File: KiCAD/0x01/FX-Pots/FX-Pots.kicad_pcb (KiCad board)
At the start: 2 copper layers, 100 x 100 mm, 41 parts, among them J1 IN, J2 OUT, SW1 SW_Push_LED, SW2 SW_Push_LED, SW3 SW_Push_LED, SW4 SW_Push_LED, SW5 SW_Push_LED, SW6 SW_Push_LED, SW7 SW_Push_LED, SW8 SW_Push_LED, U1 ADS7830, U2 HT16K33 24SOP

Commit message: fixes
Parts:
- U2: footprint Package_SO:SSOP-24_5.3x8.2mm_P0.65mm -> Package_SO:SOIC-24W_7.5x15.4mm_P1.27mm
- moved C2 2.68 mm to (153.0, 81.5)
- moved D2 1.69 mm to (152.5, 100.5)
- moved D3 1.69 mm to (154.6, 100.5)
- moved C3 0.49 mm to (154.2, 112.5)
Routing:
- net GND: track 132.0 -> 15.2 mm, vias 8 -> 4
- net +5V: track 70.3 -> 4.73 mm, vias 8 -> 3
- net /A1_H: track 85.9 -> 111.1 mm
- net /R3: track 107.9 -> 128.5 mm, vias 0 -> 1
- net /SDA: track 108.2 -> 125.5 mm
- net /POT7: track 59.5 -> 43.0 mm, vias 1 -> 0
- net /POT5: track 62.9 -> 75.7 mm, vias 1 -> 2
- net /R5: track 115.4 -> 125.8 mm, vias 0 -> 1
- net /COM0: track 154.5 -> 164.5 mm, vias 1 -> 2
- net /R2: track 46.9 -> 56.2 mm
- net Net-(D2-K): track 175.0 -> 183.1 mm
- net /SCL: track 108.6 -> 116.4 mm, vias 2 -> 4
- net /R8: track 29.5 -> 22.0 mm, vias 0 -> 2
- net /A0_H: track 73.8 -> 67.8 mm
- net /R6: track 111.9 -> 116.9 mm
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
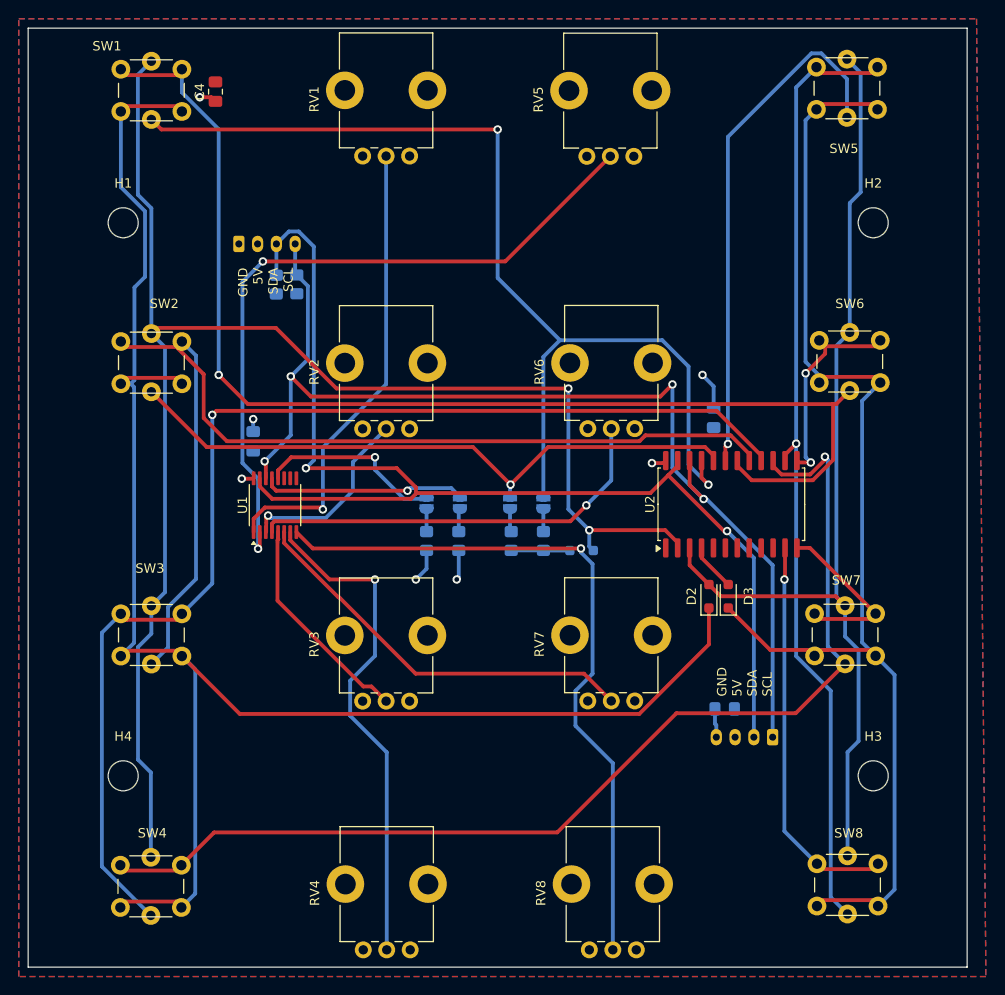
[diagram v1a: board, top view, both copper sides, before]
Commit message: fx-pots refactoring WIP
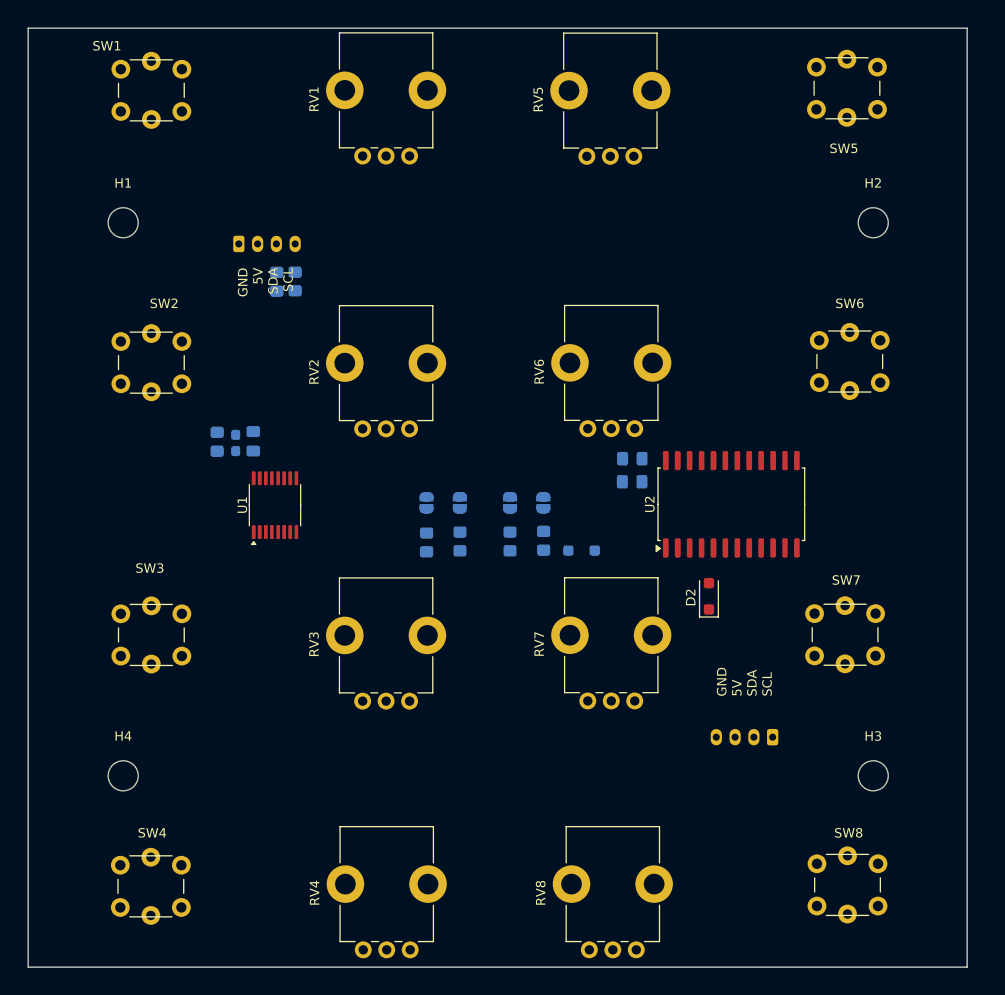
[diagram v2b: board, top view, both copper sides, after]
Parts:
- removed D3: 1N4148, Diode_SMD:D_SOD-323_HandSoldering
- added R7: 47K, Resistor_SMD:R_0805_2012Metric_Pad1.20x1.40mm_HandSolder, B.Cu at (134.9, 94.6)
- C2: value 10uF -> 1uF; footprint Capacitor_SMD:C_0805_2012Metric_Pad1.18x1.45mm_HandSolder -> Capacitor_SMD:C_0603_1608Metric_Pad1.08x0.95mm_HandSolder
- C4: value 10uF -> 1uF; moved to B.Cu
- D1, D2: footprint Diode_SMD:D_SOD-323_HandSoldering -> Diode_SMD:D_SOD-123F
- R1: value 10K -> 5R
- R3, R4: value 47K -> 10K
- R6: value 10K -> 47K
- moved C4 59.2 mm to (144.3, 85.9), turned to 180 degrees
- moved C2 51.0 mm to (102.1, 84.2)
- moved R3 36.0 mm to (108.4, 67.0), turned to 90 degrees
- moved C3 26.1 mm to (144.3, 88.3)
- moved R1 17.9 mm to (100.1, 84.0), turned to -90 degrees
- moved R4 12.4 mm to (122.4, 94.8)
- moved R6 5.46 mm to (131.3, 94.7)
- moved R5 3.56 mm to (126.0, 94.7)
- moved R2 2.15 mm to (106.5, 67.0)
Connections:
- C1 pad 1: +5V -> Net-(U1-VDD)
- C2 pad 1: +5V -> Net-(U1-VDD)
- R1 pad 2: /SDA -> Net-(U1-VDD)
- R2 pad 2: /SCL -> /SDA
- R3 pad 1: Net-(JP3-B) -> +5V
- R3 pad 2: Net-(D1-K) -> /SCL
- R4 pad 1: Net-(JP4-B) -> Net-(JP1-B)
- R4 pad 2: Net-(D1-K) -> GND
- R5 pad 1: Net-(JP1-B) -> Net-(JP2-B)
- R6 pad 1: Net-(JP2-B) -> Net-(JP3-B)
- R6 pad 2: GND -> Net-(D1-K)
- SW1 pad 1: /R3 -> /R2
- SW1 pad 4: /A1_H -> /R2
- SW2 pad 1: /R4 -> /R3
- SW2 pad 4: /A0_H -> /R3
- SW3 pad 1: /R5 -> /R4
- SW4 pad 1: /R6 -> /R5
- SW5 pad 1: /R7 -> /R6
- SW5 pad 2: Net-(D3-K) -> Net-(D2-K)
- SW5 pad 3: /COM1 -> /COM0
- SW5 pad 4: /R2 -> /R6
- SW6 pad 1: /R8 -> /R7
- SW6 pad 2: Net-(D3-K) -> Net-(D2-K)
- SW6 pad 3: /COM1 -> /COM0
- SW6 pad 4: /R3 -> /R7
- SW7 pad 1: /R9 -> /R8
- SW7 pad 2: Net-(D3-K) -> Net-(D2-K)
- SW7 pad 3: /COM1 -> /COM0
- SW7 pad 4: /R6 -> /R8
- SW8 pad 1: /R10 -> /R9
- SW8 pad 2: Net-(D3-K) -> Net-(D2-K)
- SW8 pad 3: /COM1 -> /COM0
- SW8 pad 4: /R7 -> /R9
- U1 pad 16: +5V -> Net-(U1-VDD)
- U2 pad 11: /R10 -> unconnected-(U2-ROW10/K9-Pad11)
- U2 pad 4: /COM2 -> unconnected-(U2-COM2/KS1-Pad4)
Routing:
- net Net-(D2-K): track 183.1 -> 0.00 mm
- net /COM0: track 164.5 -> 0.00 mm, vias 2 -> 0
- net Net-(D3-K): track 129.3 -> 0.00 mm
- net /R3: track 128.5 -> 0.00 mm, vias 1 -> 0
- net /R5: track 125.8 -> 0.00 mm, vias 1 -> 0
- net /SDA: track 125.5 -> 0.00 mm, vias 2 -> 0
- net /R6: track 116.9 -> 0.00 mm, vias 1 -> 0
- net /SCL: track 116.4 -> 0.00 mm, vias 4 -> 0
- net /R4: track 113.6 -> 0.00 mm
- net /A1_H: track 111.1 -> 0.00 mm, vias 2 -> 0
- net /COM1: track 108.2 -> 0.00 mm
- net /R7: track 102.7 -> 0.00 mm, vias 1 -> 0
- net /POT8: track 76.7 -> 0.00 mm, vias 1 -> 0
- net /POT5: track 75.7 -> 0.00 mm, vias 2 -> 0
- net /A0_H: track 67.8 -> 0.00 mm, vias 1 -> 0
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- removed copper zone on B.Cu, net +5V
- removed copper zone on F.Cu, net GND

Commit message: fxpots wip
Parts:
- removed J2: OUT, Connector_JST:JST_PH_S4B-PH-K_1x04_P2.00mm_Horizontal
- added C5: 100nF, Capacitor_SMD:C_0603_1608Metric_Pad1.08x0.95mm_HandSolder, F.Cu at (108.0, 84.0)
- C4: footprint Capacitor_SMD:C_0805_2012Metric_Pad1.18x1.45mm_HandSolder -> Capacitor_SMD:C_0603_1608Metric_Pad1.08x0.95mm_HandSolder
- R1: value 5R -> 10K
- R3: value 10K -> 5R
- moved R3 19.0 mm to (100.1, 84.1), turned to -90 degrees
- moved R1 18.4 mm to (106.4, 66.8), turned to 90 degrees
- moved R2 1.99 mm to (108.5, 66.8)
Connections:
- C1 pad 1: Net-(U1-VDD) -> Net-(U1-REFin/REFout)
- C2 pad 1: Net-(U1-VDD) -> Net-(U1-REFin/REFout)
- R1 pad 2: Net-(U1-VDD) -> /SDA
- R2 pad 2: /SDA -> /SCL
- R3 pad 2: /SCL -> Net-(U1-REFin/REFout)
- U1 pad 10: unconnected-(U1-REFin/REFout-Pad10) -> Net-(U1-REFin/REFout)
- U1 pad 16: Net-(U1-VDD) -> Net-(U1-REFin/REFout)
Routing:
- net Net-(D2-K): track 0.00 -> 363.9 mm, vias 0 -> 2
- net /COM0: track 0.00 -> 333.8 mm
- net +5V: track 0.00 -> 283.7 mm, vias 0 -> 2
- net GND: track 0.00 -> 190.7 mm, vias 0 -> 7
- net /R2: track 0.00 -> 113.2 mm
- net /R3: track 0.00 -> 108.8 mm, vias 0 -> 1
- net /R5: track 0.00 -> 107.3 mm, vias 0 -> 1
- net /SCL: track 0.00 -> 98.2 mm, vias 0 -> 1
- net /SDA: track 0.00 -> 96.9 mm
- net /POT5: track 0.00 -> 86.8 mm
- net /POT8: track 0.00 -> 81.9 mm
- net /R4: track 0.00 -> 81.5 mm, vias 0 -> 1
- net /POT1: track 0.00 -> 62.9 mm
- net /R6: track 0.00 -> 55.1 mm
- net /POT7: track 0.00 -> 51.8 mm
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- added copper zone on B.Cu, net GND
- added copper zone on F.Cu, net GND

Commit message: pre firm
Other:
- board text added: "R3M1XXX 0x01 FX-POTS"
